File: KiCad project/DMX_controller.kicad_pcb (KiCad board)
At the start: 2 copper layers, 139.7 x 121.9 mm, 12 parts, among them J1 DMX_output, SW1 SW_Push_DPDT, U1 TTL_to_RS485_transceiver

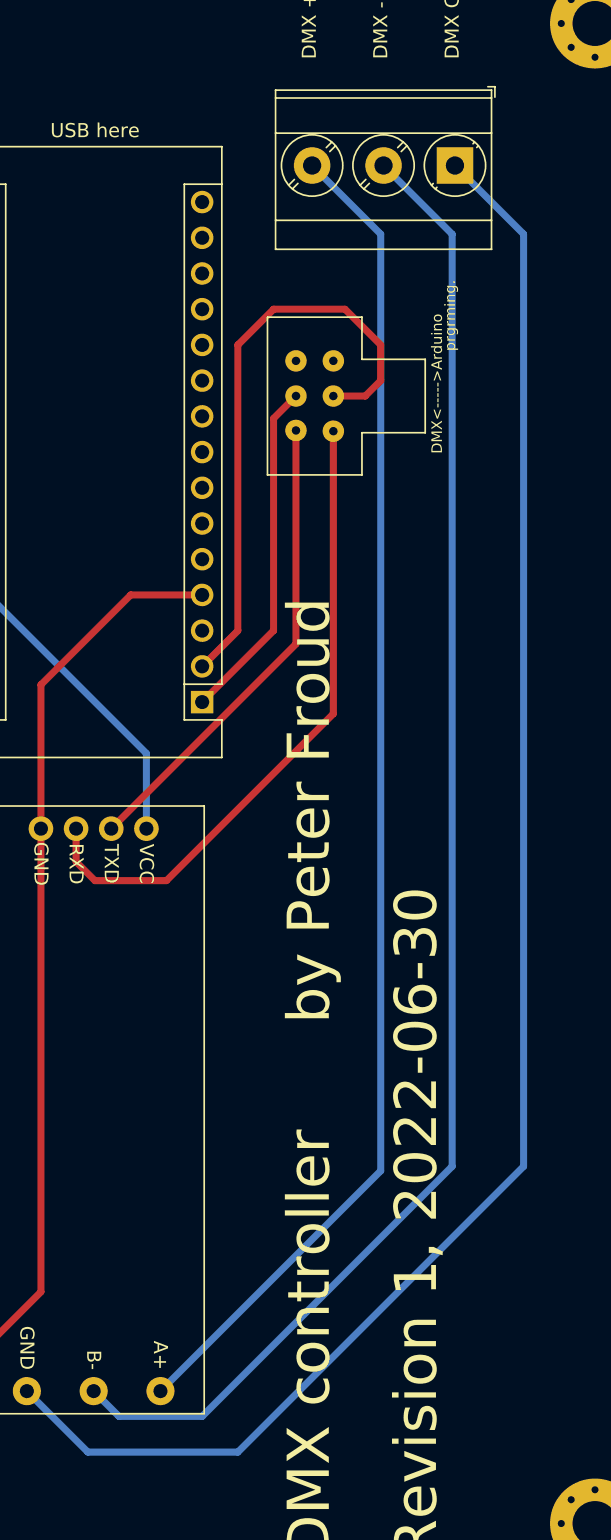
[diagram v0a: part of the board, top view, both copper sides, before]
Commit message: Route DMX (RS-485) as differential pair
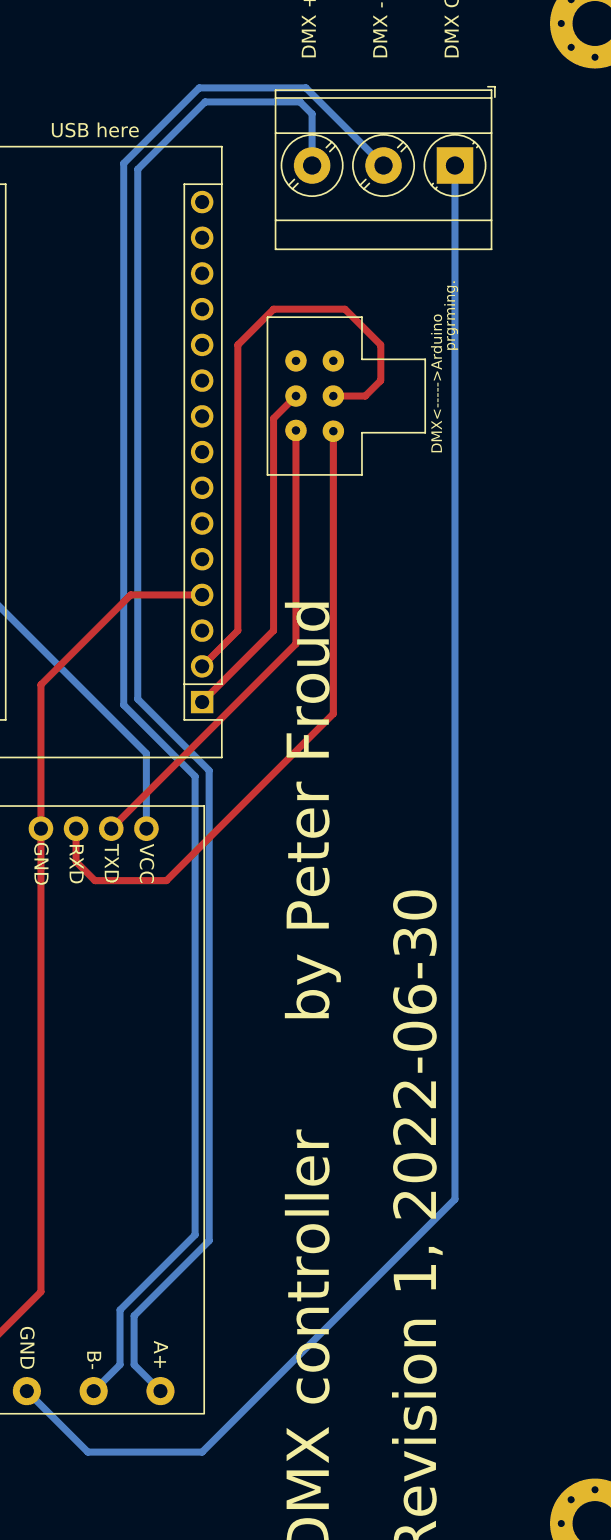
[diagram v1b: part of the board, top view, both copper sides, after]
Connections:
- net Net-(J1-Pad2) renamed /DMX-
- net Net-(J1-Pad3) renamed /DMX+
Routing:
- net /DMX+: track 95.7 -> 110.4 mm
- net /DMX-: track 106.8 -> 115.4 mm
- net Net-(J1-Pad1): track 118.7 -> 113.2 mm
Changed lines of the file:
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@@
   (net 29 "unconnected-(A1-Pad30)")
   (net 30 "Net-(J1-Pad1)")
-  (net 31 "Net-(J1-Pad2)")
-  (net 32 "Net-(J1-Pad3)")
+  (net 31 "/DMX-")
+  (net 32 "/DMX+")
   (net 33 "Net-(SW1-Pad1)")
   (net 34 "unconnected-(SW1-Pad3)")
@@
       (net 4 "GND") (pinfunction "GND") (pintype "power_in"))
     (pad "5" thru_hole circle (at 41.5 3 180) (size 2 2) (drill 1) (layers *.Cu *.Mask)
-      (net 32 "Net-(J1-Pad3)") (pinfunction "A+") (pintype "output"))
+      (net 32 "/DMX+") (pinfunction "A+") (pintype "output"))
     (pad "6" thru_hole circle (at 41.5 7.75 180) (size 2 2) (drill 1) (layers *.Cu *.Mask)
-      (net 31 "Net-(J1-Pad2)") (pinfunction "B-") (pintype "output"))
+      (net 31 "/DMX-") (pinfunction "B-") (pintype "output"))
     (pad "7" thru_hole circle (at 41.5 12.5 180) (size 2 2) (drill 1) (layers *.Cu *.Mask)
       (net 30 "Net-(J1-Pad1)") (pinfunction "GND") (pintype "power_in"))
@@
       (net 30 "Net-(J1-Pad1)") (pinfunction "Pin_1") (pintype "passive"))
     (pad "2" thru_hole circle (at 5.08 0 180) (size 2.6 2.6) (drill 1.3) (layers *.Cu *.Mask)
-      (net 31 "Net-(J1-Pad2)") (pinfunction "Pin_2") (pintype "passive"))
+      (net 31 "/DMX-") (pinfunction "Pin_2") (pintype "passive"))
     (pad "3" thru_hole circle (at 10.16 0 180) (size 2.6 2.6) (drill 1.3) (layers *.Cu *.Mask)
-      (net 32 "Net-(J1-Pad3)") (pinfunction "Pin_3") (pintype "passive"))
+      (net 32 "/DMX+") (pinfunction "Pin_3") (pintype "passive"))
     (model "${KICAD6_3DMODEL_DIR}/TerminalBlock_Phoenix.3dshapes/TerminalBlock_Phoenix_MKDS-3-3-5.08_1x03_P5.08mm_Horizontal.wrl"
       (offset (xyz 0 0 0))
@@
   (segment (start 134.62 83.82) (end 145.895255 95.095255) (width 0.5) (layer "B.Cu") (net 27))
   (segment (start 101.655 61.825) (end 84.115 61.825) (width 0.5) (layer "B.Cu") (net 27))
-  (segment (start 172.72 58.16) (end 172.72 124.46) (width 0.5) (layer "B.Cu") (net 30))
-  (segment (start 152.4 144.78) (end 172.72 124.46) (width 0.5) (layer "B.Cu") (net 30))
   (segment (start 141.733306 144.78) (end 137.395255 140.441949) (width 0.5) (layer "B.Cu") (net 30))
-  (segment (start 152.4 144.78) (end 141.733306 144.78) (width 0.5) (layer "B.Cu") (net 30))
-  (segment (start 172.72 58.16) (end 167.84 53.28) (width 0.5) (layer "B.Cu") (net 30))
-  (segment (start 167.64 58.16) (end 167.64 124.46) (width 0.5) (layer "B.Cu") (net 31))
-  (segment (start 143.943306 142.24) (end 142.145255 140.441949) (width 0.5) (layer "B.Cu") (net 31))
-  (segment (start 167.64 58.16) (end 162.76 53.28) (width 0.5) (layer "B.Cu") (net 31))
-  (segment (start 149.86 142.24) (end 143.943306 142.24) (width 0.5) (layer "B.Cu") (net 31))
-  (segment (start 149.86 142.24) (end 167.64 124.46) (width 0.5) (layer "B.Cu") (net 31))
-  (segment (start 162.56 124.777204) (end 162.56 58.16) (width 0.5) (layer "B.Cu") (net 32))
-  (segment (start 162.56 58.16) (end 157.68 53.28) (width 0.5) (layer "B.Cu") (net 32))
-  (segment (start 146.895255 140.441949) (end 162.56 124.777204) (width 0.5) (layer "B.Cu") (net 32))
+  (segment (start 167.84 53.28) (end 167.84 126.8) (width 0.5) (layer "B.Cu") (net 30))
+  (segment (start 167.84 126.8) (end 149.86 144.78) (width 0.5) (layer "B.Cu") (net 30))
+  (segment (start 149.86 144.78) (end 141.733306 144.78) (width 0.5) (layer "B.Cu") (net 30))
+  (segment (start 149.36 96.727108) (end 149.36 129.332892) (width 0.5) (layer "B.Cu") (net 31))
+  (segment (start 144.28 53.132892) (end 144.28 91.647108) (width 0.5) (layer "B.Cu") (net 31))
+  (segment (start 144.020255 138.566949) (end 142.145255 140.441949) (width 0.5) (layer "B.Cu") (net 31))
+  (segment (start 157.24 47.76) (end 149.652892 47.76) (width 0.5) (layer "B.Cu") (net 31))
+  (segment (start 144.28 91.647108) (end 149.36 96.727108) (width 0.5) (layer "B.Cu") (net 31))
+  (segment (start 149.36 129.332892) (end 144.020255 134.672637) (width 0.5) (layer "B.Cu") (net 31))
+  (segment (start 162.76 53.28) (end 157.24 47.76) (width 0.5) (layer "B.Cu") (net 31))
+  (segment (start 144.020255 134.672637) (end 144.020255 138.566949) (width 0.5) (layer "B.Cu") (net 31))
+  (segment (start 149.652892 47.76) (end 144.28 53.132892) (width 0.5) (layer "B.Cu") (net 31))
+  (segment (start 150.36 129.747108) (end 145.020255 135.086853) (width 0.5) (layer "B.Cu") (net 32))
+  (segment (start 157.68 49.614214) (end 156.825786 48.76) (width 0.5) (layer "B.Cu") (net 32))
+  (segment (start 150.067108 48.76) (end 145.28 53.547108) (width 0.5) (layer "B.Cu") (net 32))
+  (segment (start 145.28 91.232892) (end 150.36 96.312892) (width 0.5) (layer "B.Cu") (net 32))
+  (segment (start 145.020255 138.566949) (end 146.895255 140.441949) (width 0.5) (layer "B.Cu") (net 32))
+  (segment (start 145.020255 135.086853) (end 145.020255 138.566949) (width 0.5) (layer "B.Cu") (net 32))
+  (segment (start 157.68 53.28) (end 157.68 49.614214) (width 0.5) (layer "B.Cu") (net 32))
+  (segment (start 145.28 53.547108) (end 145.28 91.232892) (width 0.5) (layer "B.Cu") (net 32))
+  (segment (start 150.36 96.312892) (end 150.36 129.747108) (width 0.5) (layer "B.Cu") (net 32))
+  (segment (start 156.825786 48.76) (end 150.067108 48.76) (width 0.5) (layer "B.Cu") (net 32))
   (segment (start 143.395255 100.441949) (end 156.5325 87.304704) (width 0.5) (layer "F.Cu") (net 33))
   (segment (start 156.5325 87.304704) (end 156.5325 72.1225) (width 0.5) (layer "F.Cu") (net 33))

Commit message: Add CERN Open Hardware License Strongly Reciprocal
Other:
- board text added: "Copyright 2022 Peter Froud and others. Licensed under CERN-OHL-S v2. Source location: https://github.com/pfroud/DMX-controller"
- board text added: "Copyright Peter Froud 2022. This source describes Open Hardware and is licensed under the CERN-OHL-S v2. You may redistribute and modify this source and make products using it under the terms of the CERN-OHL-S v2 (https://ohwr.org/cern_ohl_s_v2.txt). This source is distributed WITHOUT ANY EXPRESS OR IMPLIED WARRANTY, INCLUDING OF MERCHANTABILITY, SATISFACTORY QUALITY AND FITNESS FOR A PARTICULAR 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"
- board text removed: "by Peter Froud"
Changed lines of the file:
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@@
   )
   (gr_rect (start 45.72 35.56) (end 185.42 157.48) (layer "Edge.Cuts") (width 0.1) (fill none))
-  (gr_text "by Peter Froud" (at 157.48 114.3 90) (layer "F.SilkS")
-    (effects (font (size 3 3) (thickness 0.3)) (justify left))
-  )
   (gr_text "prgrming." (at 167.499928 63.948531 90) (layer "F.SilkS")
     (effects (font (size 0.75 0.75) (thickness 0.1)))
@@
     (effects (font (size 4 4) (thickness 0.15)) (justify left))
   )
+  (gr_text "Copyright 2022 Peter Froud and others.\nLicensed under CERN-OHL-S v2.\nSource location: https://github.com/pfroud/DMX-controller" (at 177.8 139.7 90) (layer "F.SilkS")
+    (effects (font (size 1 1) (thickness 0.15)) (justify left))
+  )
+  (gr_text "Copyright Peter Froud 2022.\n\nThis source describes Open Hardware and is licensed under the CERN-OHL-S v2.\n\nYou may redistribute and modify this source and make products using it under\nthe terms of the CERN-OHL-S v2 (https://ohwr.org/cern_ohl_s_v2.txt).\n\nThis source is distributed WITHOUT ANY EXPRESS OR IMPLIED WARRANTY,\nINCLUDING OF MERCHANTABILITY, SATISFACTORY QUALITY AND FITNESS FOR A\nPARTICULAR PURPOSE. Please see the CERN-OHL-S v2 for applicable conditions. \n\nSource location: https://github.com/pfroud/DMX-controller" (at 15.24 190.5) (layer "Eco1.User")
+    (effects (font (size 1 1) (thickness 0.15)) (justify left))
+  )
   (segment (start 149.86 91.44) (end 154.94 86.36) (width 0.5) (layer "F.Cu") (net 1))

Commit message: Update PCB
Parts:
- moved SW1 4.97 mm to (157.5, 71.1)
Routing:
- net /RX: track 42.5 -> 39.8 mm
- net Net-(SW1-Pad4): track 46.2 -> 47.7 mm
- net Net-(SW1-Pad1): track 33.8 -> 35.2 mm
- net /TX: track 24.5 -> 25.5 mm
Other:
- board text added: "Revision 2, YYYY-MM-DD"
- board text removed: "Revision 1, 2022-06-30"

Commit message: Update PCB
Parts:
- moved U1 4.31 mm to (145.6, 98.7)
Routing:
- net Net-(SW1-Pad4): track 47.7 -> 49.6 mm
- net +5V: track 102.9 -> 101.0 mm
- net /DMX-: track 115.4 -> 114.0 mm
- net /DMX+: track 110.4 -> 109.0 mm
- net Net-(J1-Pad1): track 113.2 -> 114.5 mm
